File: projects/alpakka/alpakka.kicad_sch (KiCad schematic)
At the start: 76 parts, among them P1 Debug, P2 Endpoint, P3 Conn_01x02, Q1 Q_PMOS_DGS, U1 Raspberry_Pico, U10 ST_LSM6, U12 ST_LSM6, U2 Alpsalpine_RKJXV, U3 Alpsalpine_EC10E, U4 Alpsalpine_RKJXM, U6 NXP_PCAL6416A, U8 NXP_PCAL6416A

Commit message: Alpakka board RF proto
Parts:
- removed Q1: Q_PMOS_DGS, ILO_fp:SOT-23-DGS, symbol Device:Q_PMOS_DGS
- removed TP10, TP11, TP12, TP14, TP15, TP16, TP19, TP20, TP24, TP25, TP26, TP3, TP33, TP35, TP36, TP4, TP5, TP6, TP7, TP9: Endpoint, ILO_fp:Pad_1mm, symbol ILO_sym:Endpoint
- removed U1: Raspberry_Pico, ILO_fp:Raspberry_Pico, symbol ILO_sym:Raspberry_Pico
- removed U4: Alpsalpine_RKJXM, ILO_fp:Alpsalpine_RKJXM1015004, symbol ILO_sym:Alpsalpine_RKJXM
- added C3, C4: 100pF, ILO_fp:0402, symbol Device:C
- added J1, J2: Conn_01x20_Pin, ILO_fp:Hirose_DF12NB_receptacle, symbol Connector:Conn_01x20_Pin
- added TPA2, TPA3, TPP0, TPP1, TPS0, TPS1: Endpoint, ILO_fp:Pad_1mm, symbol ILO_sym:Endpoint
- added U2: Alpsalpine_RKJXV, ILO_fp:Alpsalpine_RKJXV122400R, symbol ILO_sym:Alpsalpine_RKJXV
- C1, C2: value C -> 100pF
- C5: renamed from C4; value C -> 100pF
- C6: renamed from C3; value C -> 100pF
- C7: renamed from C6; value C -> 100pF
- C8: renamed from C5; value C -> 100pF
- P2: value Endpoint -> Blade
- P3: Group (none) -> Power
- R1, R2, R3, R4: value R -> 20 Ω; Group R_20 -> R
- R6: value R6 -> 2 MΩ; Group R_500K -> R; LCSC C11616 -> C138014
- S15, S16, U3: Export (none) -> yes
- U1: renamed from U2; Export (none) -> yes
- renumbered TP31 to TPA0, TP32 to TPA1
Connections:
- net GNDA is gone; now on net GND: U10.7 (GND), U12.7 (GND)
- net GP2 is gone; now on net GP6: D4.2 (A)
- net GP3 is gone; now on net GP7: D3.2 (A)
- net GP4 is gone; now on net GP9: D1.2 (A)
- net GP5 is gone; now on net GP8: D2.2 (A)
- net VCCA is gone; now on net VCC: C6.2, C8.2, U10.8 (VDD), U12.8 (VDD)
- net ADC0: now also C3.2, J2.7 (Pin_7), U2.5 (ADC1); no longer C2.2, U1.2 (ADC0)
- net ADC1: now also C4.2, J2.8 (Pin_8), U2.2 (ADC0); no longer C1.2, U1.5 (ADC1)
- net B2: now also U2.10 (D), U2.8 (B)
- net BAT: now also J1.5 (Pin_5), J1.6 (Pin_6)
- net GND: now also C3.1, C4.1, J1.3 (Pin_3), J1.4 (Pin_4), J1.7 (Pin_7), J1.8 (Pin_8), J2.15 (Pin_15), J2.16 (Pin_16), J2.17 (Pin_17), J2.18 (Pin_18), J2.19 (Pin_19), J2.20 (Pin_20), TPP0.1, U2.1 (GND0), U2.4 (GND1), U2.7 (A), U2.9 (C); no longer U6.13 (P11)
- net GP6: now also J1.18 (Pin_18); no longer R6.1
- net GP7: now also J1.17 (Pin_17); no longer P2.1, R6.2
- net GP8: now also J1.16 (Pin_16); no longer U3.2 (B)
- net GP9: now also J1.15 (Pin_15); no longer U3.1 (A)
- net I2C_SCL: now also J2.2 (Pin_2)
- net I2C_SDA: now also J2.1 (Pin_1)
- net RUN: now also J2.14 (Pin_14)
- net SPI_CK: now also J2.11 (Pin_11)
- net SPI_RX: now also J2.13 (Pin_13)
- net SPI_TX: now also J2.12 (Pin_12)
- net UART_RX: now also J1.9 (Pin_9)
- net UART_TX: now also J1.10 (Pin_10)
- net VCC: now also J1.1 (Pin_1), J1.2 (Pin_2), TPP1.1, U2.3 (VCC0), U2.6 (VCC1)
- net CS0 renamed IMU_CS0
- net IMU_CS0: now also J1.20 (Pin_20)
- net CS1 renamed IMU_CS1
- net IMU_CS1: now also J1.19 (Pin_19)
- net GP20 renamed GP23
- net GP23: now also J2.4 (Pin_4)
- new net A11: U6.13 (P11)
- new net ADC2: C1.2, J2.9 (Pin_9), TPA2.1, U1.5 (ADC1)
- new net ADC3: C2.2, J2.10 (Pin_10), TPA3.1, U1.2 (ADC0)
- new net GP10: J1.14 (Pin_14), TPS0.1, U3.1 (A)
- new net GP11: J1.13 (Pin_13), TPS1.1, U3.2 (B)
- new net GP12: J1.12 (Pin_12), P2.1, R6.2
- new net GP13: J1.11 (Pin_11), R6.1
- new net GP22: J2.3 (Pin_3)
- new net GP24: J2.5 (Pin_5)
- new net GP25: J2.6 (Pin_6)
- no-connect marks 26 -> 18
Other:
- note added: "CONNECTORS TO MCU BOARD"
- note removed: "DIRECTIONAL SWITCH"
- moved on the sheet: C1, C2, C5, C6, C7, C8, D1, D2, D3, D4, P1, P2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

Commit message: RF test A2
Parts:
- added C11, C12: 1uF, ILO_fp:0402, symbol Device:C
- added P5: Jack 2.5mm, symbol Connector_Generic:Conn_01x03
- C1: renamed from C2; value 100pF -> 100nF; Group C_100nF -> C TS
- C2: renamed from C1; value 100pF -> 100nF; Group C_100nF -> C TS
- C3: renamed from C4; value 100pF -> 100nF; Group C_100nF -> C TS
- C4: renamed from C3; value 100pF -> 100nF; Group C_100nF -> C TS
- C5, C6, C7, C8: value 100pF -> 100nF; Group C_100nF -> C IMU
- P1: renamed from J1; Group (none) -> Core port
- P2: renamed from J2; Group (none) -> Core port
- P3: renamed from P1; value Debug -> JST PH; Group Debug -> Dev port
- P4: renamed from P2; Group Capacitive -> Touch port
- P6: renamed from P3; Group Power -> Batt port
- S15: value l1 -> L1
- S16: value r1 -> R1
- S17: value l2 -> L2
- S18: value r2 -> R2
- S19: value l4 -> L4
- S20: value r4 -> R4
- S5: value a -> A
- S6: value b -> B
- S7: value x -> X
- S8: value y -> Y
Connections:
- net GP22 is gone; now on net ADC1: P2.3 (Pin_3)
- net A10: now also S11.2
- net A12: now also P5.2 (Pin_2); no longer U1.10 (D), U1.8 (B)
- net A13: now also P5.3 (Pin_3); no longer S11.2
- net A9: now also U1.10 (D), U1.8 (B); no longer S19.2, TP204.1
- net ADC0: now also P2.4 (Pin_4); no longer P2.7 (Pin_7)
- net ADC1: no longer P2.8 (Pin_8)
- net ADC2: now also P2.2 (Pin_2), C12.2; no longer P2.9 (Pin_9)
- net ADC3: now also P2.1 (Pin_1), C11.2; no longer P2.10 (Pin_10)
- net GND: now also P2.11 (Pin_11), P2.12 (Pin_12), C11.1, C12.1, P5.1 (Pin_1); no longer P2.15 (Pin_15), P2.16 (Pin_16), P2.17 (Pin_17), P2.18 (Pin_18), P2.19 (Pin_19), P2.20 (Pin_20)
- net GP10: now also P1.17 (Pin_17); no longer P1.14 (Pin_14)
- net GP11: now also P1.18 (Pin_18); no longer P1.13 (Pin_13)
- net GP12: now also P1.19 (Pin_19); no longer P1.12 (Pin_12)
- net GP13: now also P1.20 (Pin_20); no longer P1.11 (Pin_11)
- net GP24: now also P2.6 (Pin_6), S14.2; no longer P2.5 (Pin_5)
- net GP25: now also P2.5 (Pin_5); no longer P2.6 (Pin_6)
- net GP6: now also P1.13 (Pin_13); no longer P1.18 (Pin_18)
- net GP7: now also P1.14 (Pin_14); no longer P1.17 (Pin_17)
- net GP8: now also P1.15 (Pin_15); no longer P1.16 (Pin_16)
- net GP9: now also P1.16 (Pin_16); no longer P1.15 (Pin_15)
- net I2C_SCL: now also P2.7 (Pin_7); no longer P2.2 (Pin_2)
- net I2C_SDA: now also P2.8 (Pin_8); no longer P2.1 (Pin_1)
- net IMU_CS0: now also P1.11 (Pin_11); no longer P1.20 (Pin_20)
- net IMU_CS1: now also P1.12 (Pin_12); no longer P1.19 (Pin_19)
- net RUN: now also P2.17 (Pin_17); no longer P2.14 (Pin_14)
- net SPI_CK: now also P2.20 (Pin_20); no longer P2.11 (Pin_11)
- net SPI_RX: now also P2.18 (Pin_18); no longer P2.13 (Pin_13)
- net SPI_TX: now also P2.19 (Pin_19); no longer P2.12 (Pin_12)
- net VCC: now also P1.10 (Pin_10), P1.9 (Pin_9); no longer P1.1 (Pin_1), P1.2 (Pin_2)
- net A8: now reaches U6.10 (P8)
- net A8: now also S19.2, TP204.1
- removed net GP23: P2.4 (Pin_4), S14.2
- net UART_RX renamed UART0_RX
- net UART0_RX: now also P1.2 (Pin_2); no longer P1.9 (Pin_9)
- net UART_TX renamed UART0_TX
- net UART0_TX: now also P1.1 (Pin_1); no longer P1.10 (Pin_10)
- new net UART1_RX: P2.9 (Pin_9)
- new net UART1_TX: P2.10 (Pin_10)
- no-connect marks 18 -> 21
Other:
- note added: "BUTTONS CENTER"
- note added: "PEDAL CONNECTOR"
- note added: "TOUCH SENSOR"
- note removed: "BUTTONS FRONT"
- note removed: "CAPACITIVE"
- moved on the sheet: C1, C2, C3, C4, C5, C6, D1, D2, D3, D4, P1, P2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

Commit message: RF test A2 final
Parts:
- removed C1, C2, C3, C4: 100nF, ILO_fp:0402, symbol Device:C
- renumbered C5 to C1, C6 to C2, C7 to C3, C8 to C4, C11 to C5, C12 to C6
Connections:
- net GND: no longer P1.3 (Pin_3), P1.4 (Pin_4)
- no-connect marks 21 -> 24
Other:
- moved on the sheet: C5, C6

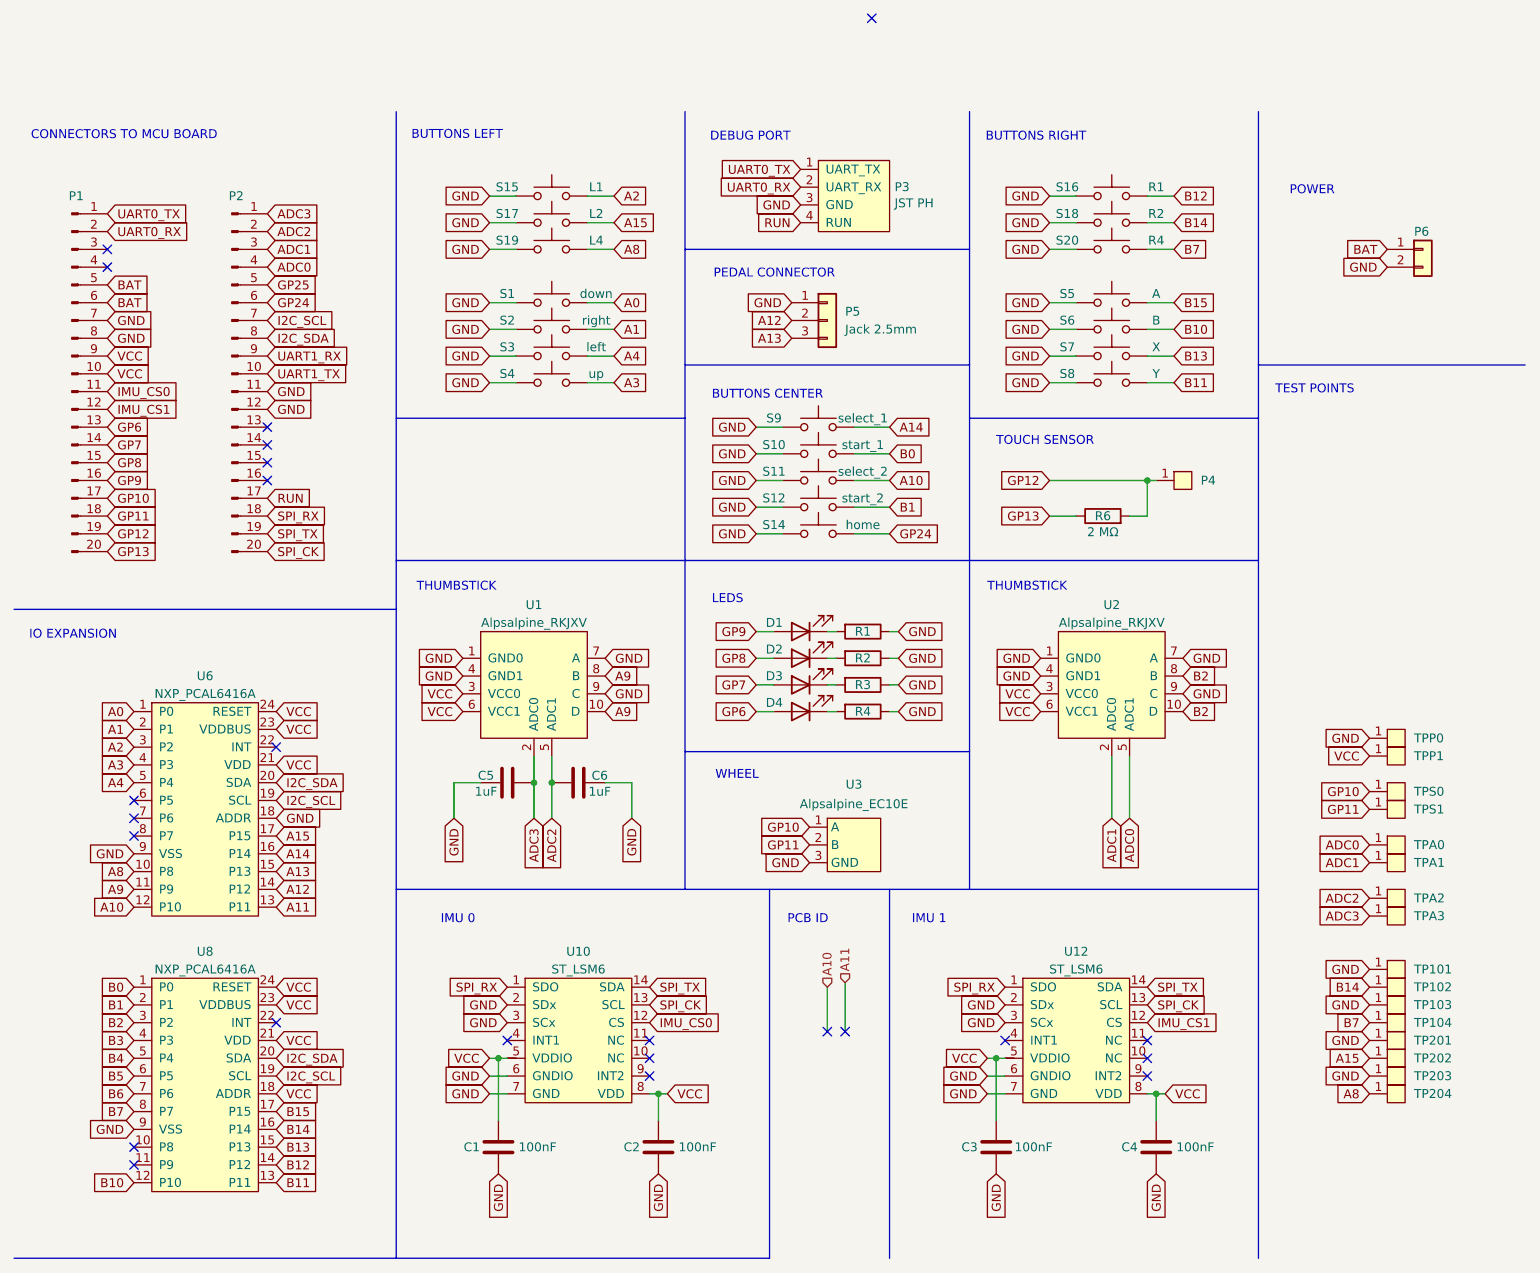
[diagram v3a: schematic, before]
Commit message: Changed debug port to header pins, Changed nets from global to local
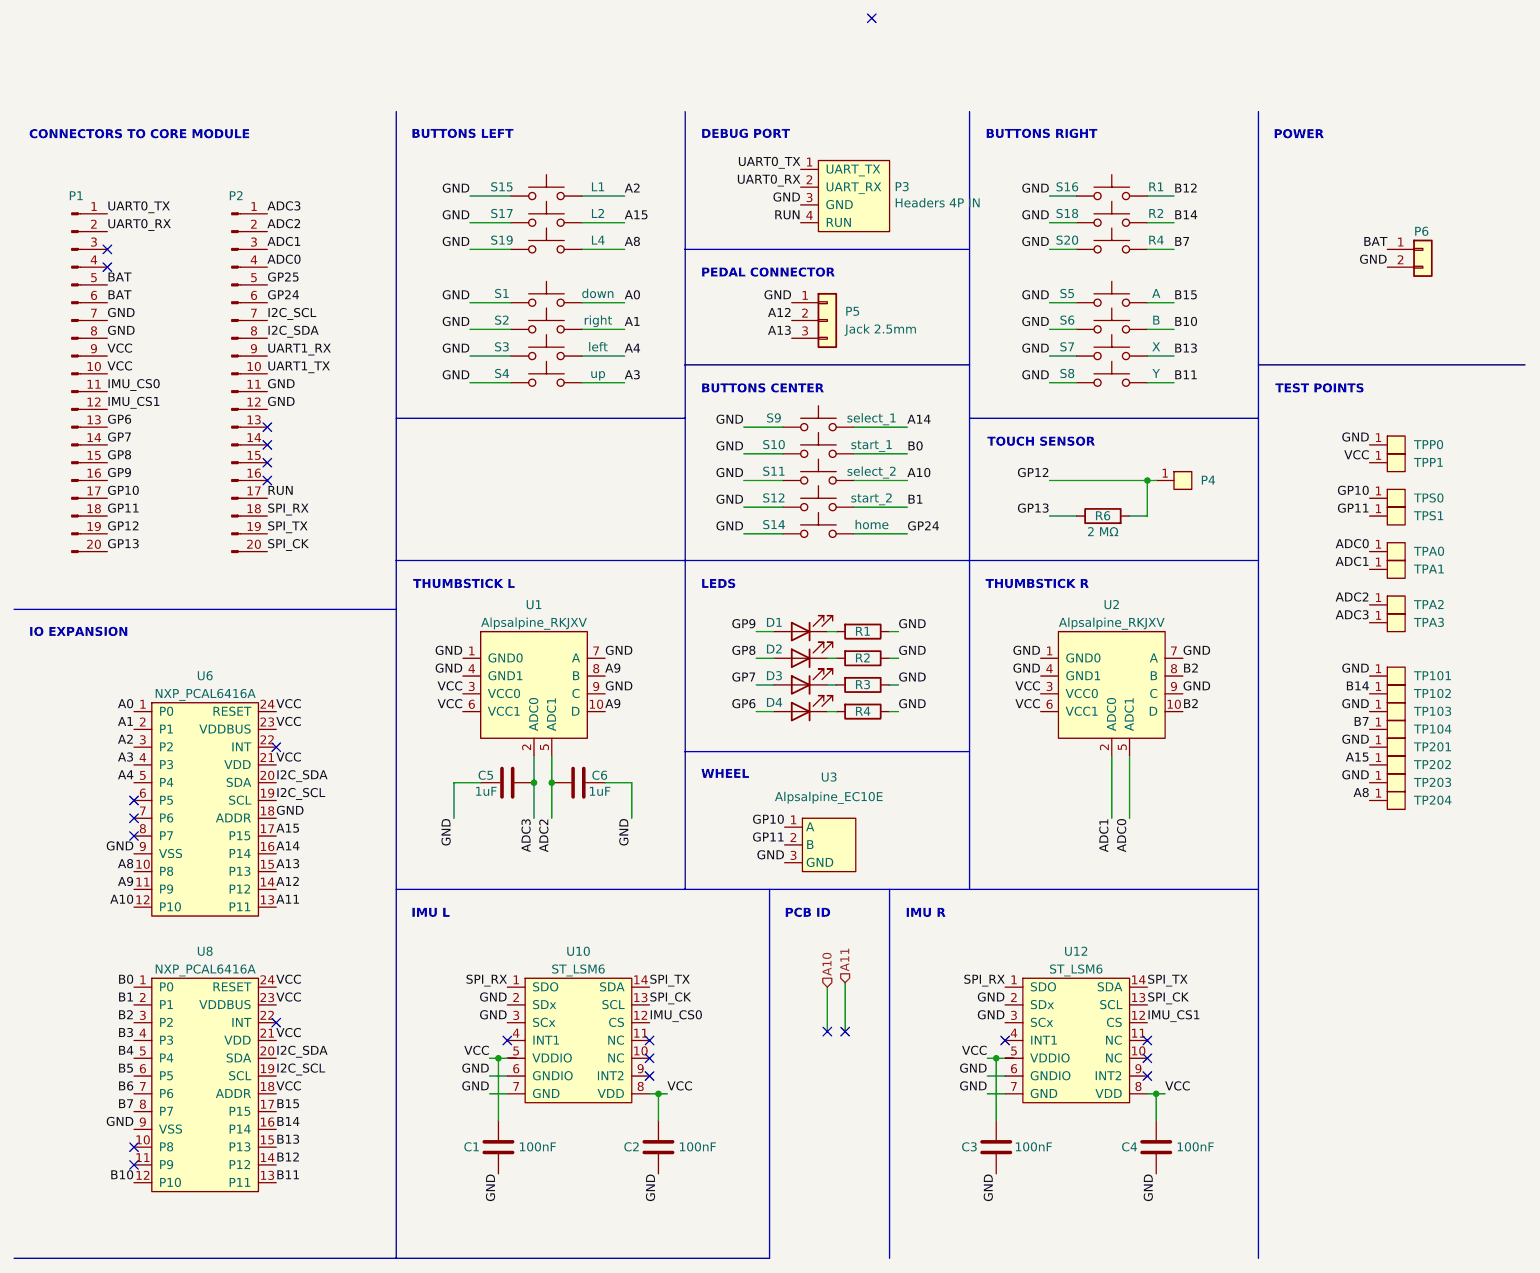
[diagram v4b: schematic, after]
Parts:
- P3: value JST PH -> Headers 4P IN; footprint ILO_fp:JST_S4B-PH-SM4-K-TB -> ILO_fp:XKB_X6511FRS-04; LCSC C265332 -> C5142237
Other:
- note added: "CONNECTORS TO CORE MODULE"
- note added: "IMU L"
- note added: "IMU R"
- note added: "THUMBSTICK L"
- note added: "THUMBSTICK R"
- note removed: "CONNECTORS TO MCU BOARD"
- note removed: "IMU 0"
- note removed: "IMU 1"
- note removed: "THUMBSTICK"
- moved on the sheet: S1, S15, S17, S19, S2, S3, S4, TP101, TP102, TP103, TP104, TP201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

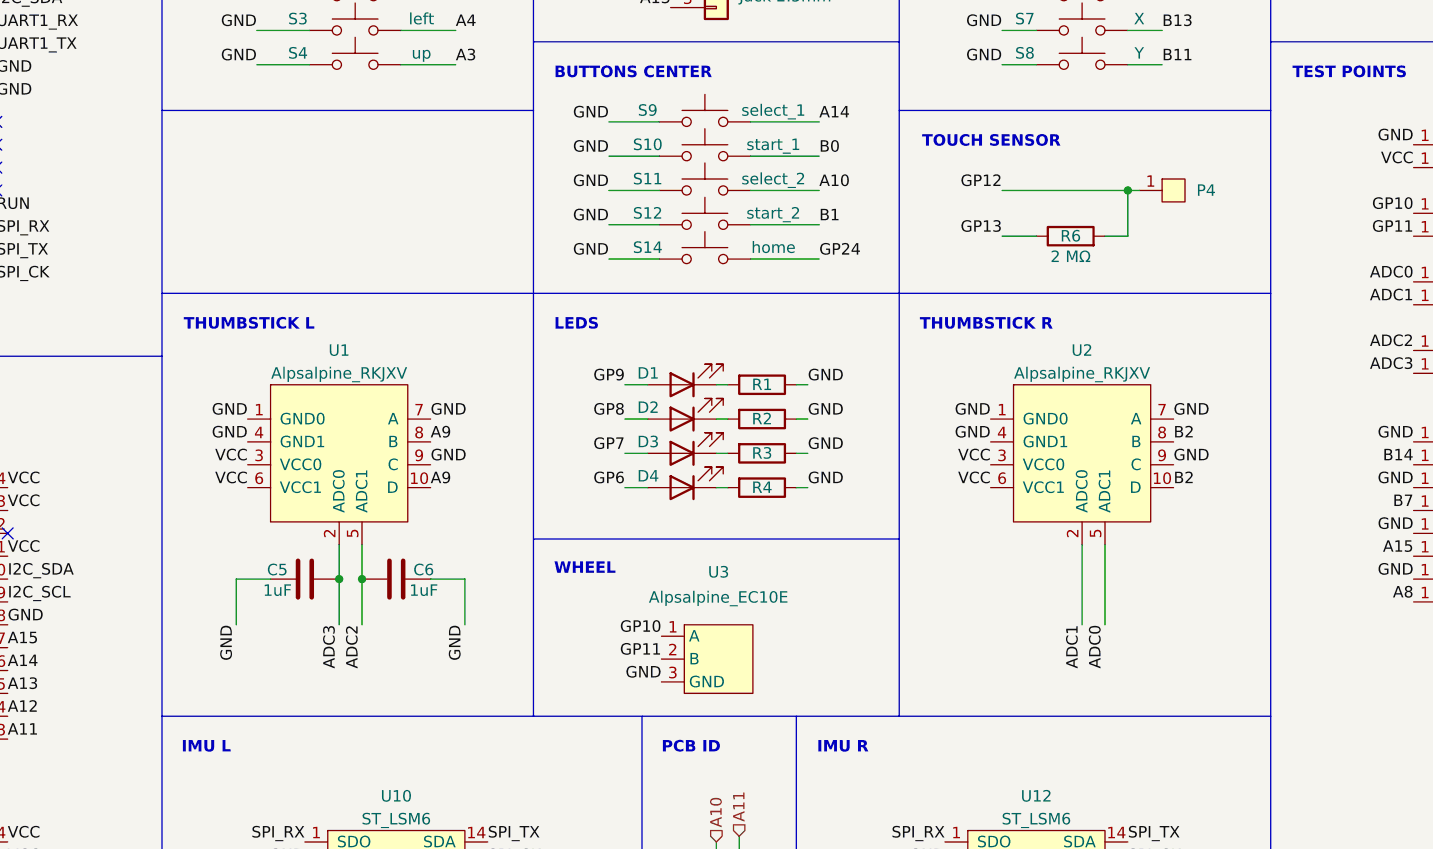
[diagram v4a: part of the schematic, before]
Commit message: 1M touch resistor with optional 500K mode
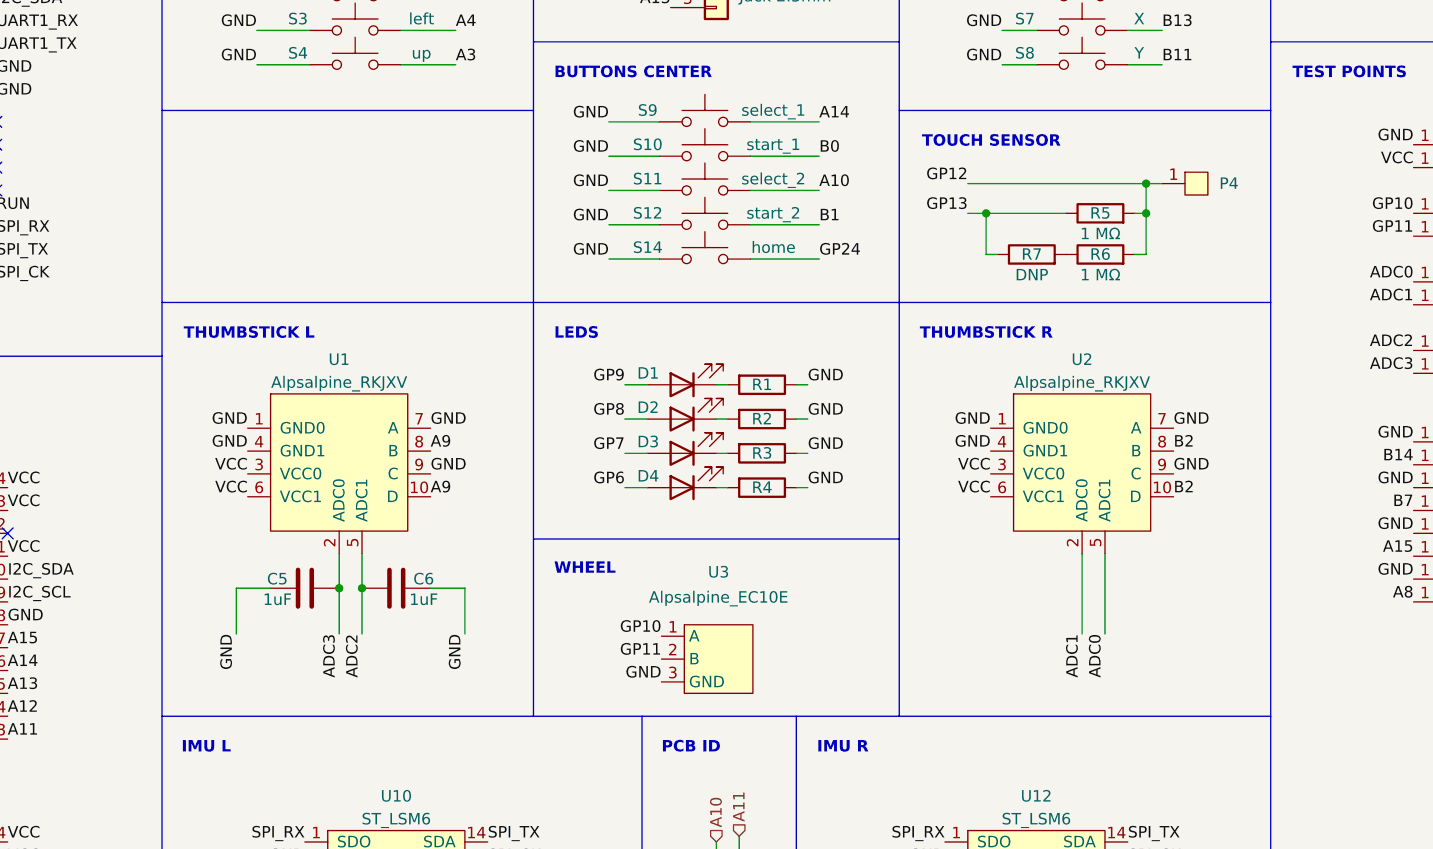
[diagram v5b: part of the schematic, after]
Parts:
- added R6: 1 MΩ, ILO_fp:0402, symbol Device:R
- added R7: DNP, ILO_fp:0603_compact, symbol Device:R
- R5: renamed from R6; value 2 MΩ -> 1 MΩ; LCSC C138014 -> C26083
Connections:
- net GP12: now also R6.2
- net GP13: now also R7.1
- new net: R6.1, R7.2
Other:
- moved on the sheet: C5, C6, P4, R5, U1, U2
